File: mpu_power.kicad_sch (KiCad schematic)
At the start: 50 parts, among them U501 STM32MP135FAE7

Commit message: Rework text boxes
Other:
- note added: "Decoupling"
- note added: "Notes"
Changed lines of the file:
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@@
 		(rev "v1.0.0")
+	)
+	(rectangle
+		(start 12.7 251.46)
+		(end 298.45 284.48)
+		(stroke
+			(width 0)
+			(type default)
+		)
+		(fill
+			(type none)
+		)
+	)
+	(rectangle
+		(start 12.7 50.8)
+		(end 406.4 251.46)
+		(stroke
+			(width 0)
+			(type default)
+		)
+		(fill
+			(type none)
+		)
 	)
 	(text "1 µF x VDD"
@@
 		)
 	)
+	(text "Notes"
+		(exclude_from_sim no)
+		(at 13.97 254 0)
+		(effects
+			(font
+				(size 5.08 5.08)
+				(thickness 1.016)
+				(bold yes)
+			)
+			(justify left top)
+		)
+	)
 	(text "1 µF x VDD_PLL + 1 µF x VDD_SD2 + 1 µF x VBAT + 1 µF x VDD_ANA"
 		(exclude_from_sim no)
@@
 			)
 			(justify left bottom)
+		)
+	)
+	(text "Decoupling"
+		(exclude_from_sim no)
+		(at 13.97 53.34 0)
+		(effects
+			(font
+				(size 5.08 5.08)
+				(thickness 1.016)
+				(bold yes)
+			)
+			(justify left top)
 		)
 	)
@@
 		)
 	)
-	(text_box "Notes"
-		(exclude_from_sim no)
-		(at 12.7 251.46 0)
-		(size 285.75 33.02)
-		(margins 0.9525 2 0.9525 0.9525)
-		(stroke
-			(width 0)
-			(type solid)
-		)
-		(fill
-			(type none)
-		)
-		(effects
-			(font
-				(size 5.08 5.08)
-				(thickness 1.016)
-				(bold yes)
-			)
-			(justify top)
-		)
-	)
-	(text_box ""
-		(exclude_from_sim no)
-		(at 12.7 50.8 0)
-		(size 393.7 200.66)
-		(margins 0.9525 2 0.9525 0.9525)
-		(stroke
-			(width 0)
-			(type solid)
-		)
-		(fill
-			(type none)
-		)
-		(effects
-			(font
-				(size 5.08 5.08)
-				(thickness 1.016)
-				(bold yes)
-			)
-			(justify top)
-		)
-	)

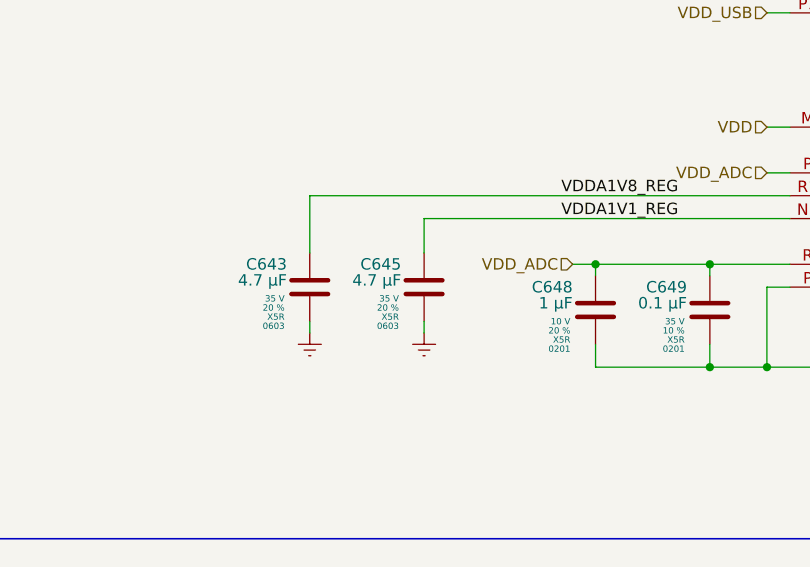
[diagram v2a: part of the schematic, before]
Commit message: Fix power connections
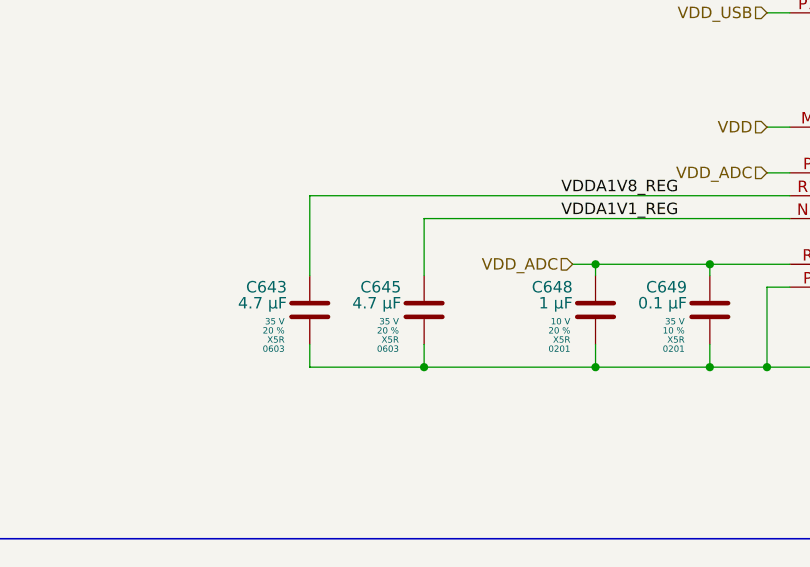
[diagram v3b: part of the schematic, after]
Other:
- moved on the sheet: C643, C645
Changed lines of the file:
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@@
 	)
 	(junction
+		(at 196.85 232.41)
+		(diameter 0)
+		(color 0 0 0 0)
+	)
+	(junction
 		(at 260.35 88.9)
 		(diameter 0)
@@
 	)
 	(junction
+		(at 177.8 232.41)
+		(diameter 0)
+		(color 0 0 0 0)
+	)
+	(junction
 		(at 53.34 177.8)
 		(diameter 0)
@@
 	(wire
 		(pts
-			(xy 177.8 215.9) (xy 177.8 219.71)
+			(xy 177.8 215.9) (xy 177.8 222.25)
 		)
 		(stroke
@@
 	(wire
 		(pts
+			(xy 165.1 232.41) (xy 177.8 232.41)
+		)
+		(stroke
+			(width 0)
+			(type default)
+		)
+	)
+	(wire
+		(pts
 			(xy 40.64 180.34) (xy 40.64 177.8)
 		)
@@
 	(wire
 		(pts
+			(xy 177.8 232.41) (xy 196.85 232.41)
+		)
+		(stroke
+			(width 0)
+			(type default)
+		)
+	)
+	(wire
+		(pts
 			(xy 78.74 165.1) (xy 91.44 165.1)
 		)
@@
 	(wire
 		(pts
+			(xy 165.1 229.87) (xy 165.1 232.41)
+		)
+		(stroke
+			(width 0)
+			(type default)
+		)
+	)
+	(wire
+		(pts
 			(xy 66.04 190.5) (xy 78.74 190.5)
 		)
@@
 	(wire
 		(pts
-			(xy 177.8 227.33) (xy 177.8 228.6)
+			(xy 177.8 229.87) (xy 177.8 232.41)
 		)
 		(stroke
@@
 	(wire
 		(pts
-			(xy 165.1 213.36) (xy 165.1 219.71)
+			(xy 165.1 213.36) (xy 165.1 222.25)
 		)
 		(stroke
@@
 	(wire
 		(pts
-			(xy 165.1 227.33) (xy 165.1 228.6)
-		)
-		(stroke
-			(width 0)
-			(type default)
-		)
-	)
-	(wire
-		(pts
 			(xy 209.55 229.87) (xy 209.55 232.41)
 		)
@@
 		(dnp no)
 		(fields_autoplaced yes)
-		(property "Reference" "#PWR0611"
+		(property "Reference" "#PWR0609"
 			(at 260.35 240.03 0)
 			(effects
@@
 			(project "linux-sbc"
 				(path "/fa11a02f-8043-4153-ab69-88d766503017/2d01087b-54dc-4f43-9cc7-a0ba17201776/38fb80ce-3aa2-4a17-bb8b-7759011755a2"
-					(reference "#PWR0611")
+					(reference "#PWR0609")
 					(unit 1)
 				)
@@
 	(symbol
 		(lib_id "Device:C")
-		(at 177.8 223.52 0)
+		(at 177.8 226.06 0)
 		(mirror y)
 		(unit 1)
@@
 		(dnp no)
 		(property "Reference" "C645"
-			(at 175.26 220.98 0)
+			(at 175.26 223.52 0)
 			(effects
 				(font
@@
 		)
 		(property "Value" "4.7 µF"
-			(at 175.26 222.758 0)
+			(at 175.26 225.298 0)
 			(effects
 				(font
@@
 		)
 		(property "Footprint" "Capacitor_SMD:C_0603_1608Metric"
-			(at 176.8348 227.33 0)
+			(at 176.8348 229.87 0)
 			(effects
 				(font
@@
 		)
 		(property "Datasheet" "https://search.murata.co.jp/Ceramy/image/img/A01X/G101/ENG/GRM188R6YA475KE15-01.pdf"
-			(at 177.8 223.52 0)
+			(at 177.8 226.06 0)
 			(effects
 				(font
@@
 		)
 		(property "Description" "4.7 µF ±10% 35V Ceramic Capacitor X5R 0603 (1608 Metric)"
-			(at 177.8 223.52 0)
+			(at 177.8 226.06 0)
 			(effects
 				(font
@@
 		)
 		(property "MPN" "GRM188R6YA475KE15D"
-			(at 177.8 223.52 0)
+			(at 177.8 226.06 0)
 			(effects
 				(font
@@
 		)
 		(property "Manufacturer" "Murata Electronics"
-			(at 177.8 223.52 0)
+			(at 177.8 226.06 0)
 			(effects
 				(font
@@
 		)
 		(property "Voltage rating" "35 V"
-			(at 175.006 224.79 0)
+			(at 175.006 227.33 0)
 			(effects
 				(font
@@
 		)
 		(property "Tolerance" "20 %"
-			(at 175.006 225.806 0)
+			(at 175.006 228.346 0)
 			(effects
 				(font
@@
 		)
 		(property "Temperature coefficient" "X5R"
-			(at 175.006 226.822 0)
+			(at 175.006 229.362 0)
 			(effects
 				(font
@@
 		)
 		(property "Size" "0603"
-			(at 175.006 227.838 0)
+			(at 175.006 230.378 0)
 			(effects
 				(font
@@
 		)
 		(property "Digi-Key Part Number" "490-7205-1-ND"
-			(at 177.8 223.52 0)
+			(at 177.8 226.06 0)
 			(effects
 				(font
@@
 	(symbol
 		(lib_id "Device:C")
-		(at 165.1 223.52 0)
+		(at 165.1 226.06 0)
 		(mirror y)
 		(unit 1)
@@
 		(dnp no)
 		(property "Reference" "C643"
-			(at 162.56 220.98 0)
+			(at 162.56 223.52 0)
 			(effects
 				(font
@@
 		)
 		(property "Value" "4.7 µF"
-			(at 162.56 222.758 0)
+			(at 162.56 225.298 0)
 			(effects
 				(font
@@
 		)
 		(property "Footprint" "Capacitor_SMD:C_0603_1608Metric"
-			(at 164.1348 227.33 0)
+			(at 164.1348 229.87 0)
 			(effects
 				(font
@@
 		)
 		(property "Datasheet" "https://search.murata.co.jp/Ceramy/image/img/A01X/G101/ENG/GRM188R6YA475KE15-01.pdf"
-			(at 165.1 223.52 0)
+			(at 165.1 226.06 0)
 			(effects
 				(font
@@
 		)
 		(property "Description" "4.7 µF ±10% 35V Ceramic Capacitor X5R 0603 (1608 Metric)"
-			(at 165.1 223.52 0)
+			(at 165.1 226.06 0)
 			(effects
 				(font
@@
 		)
 		(property "MPN" "GRM188R6YA475KE15D"
-			(at 165.1 223.52 0)
+			(at 165.1 226.06 0)
 			(effects
 				(font
@@
 		)
 		(property "Manufacturer" "Murata Electronics"
-			(at 165.1 223.52 0)
+			(at 165.1 226.06 0)
 			(effects
 				(font
@@
 		)
 		(property "Voltage rating" "35 V"
-			(at 162.306 224.79 0)
+			(at 162.306 227.33 0)
 			(effects
 				(font
@@
 		)
 		(property "Tolerance" "20 %"
-			(at 162.306 225.806 0)
+			(at 162.306 228.346 0)
 			(effects
 				(font
@@
 		)
 		(property "Temperature coefficient" "X5R"
-			(at 162.306 226.822 0)
+			(at 162.306 229.362 0)
 			(effects
 				(font
@@
 		)
 		(property "Size" "0603"
-			(at 162.306 227.838 0)
+			(at 162.306 230.378 0)
 			(effects
 				(font
@@
 		)
 		(property "Digi-Key Part Number" "490-7205-1-ND"
-			(at 165.1 223.52 0)
+			(at 165.1 226.06 0)
 			(effects
 				(font
@@
 	)
 	(symbol
-		(lib_id "power:Earth")
-		(at 177.8 228.6 0)
-		(unit 1)
-		(exclude_from_sim no)
-		(in_bom yes)
-		(on_board yes)
-		(dnp no)
-		(fields_autoplaced yes)
-		(property "Reference" "#PWR0609"
-			(at 177.8 234.95 0)
-			(effects
-				(font
-					(size 1.27 1.27)
-				)
-				(hide yes)
-			)
-		)
-		(property "Value" "GND"
-			(at 177.8 233.68 0)
-			(effects
-				(font
-					(size 1.27 1.27)
-				)
-				(hide yes)
-			)
-		)
-		(property "Footprint" ""
-			(at 177.8 228.6 0)
-			(effects
-				(font
-					(size 1.27 1.27)
-				)
-				(hide yes)
-			)
-		)
-		(property "Datasheet" "~"
-			(at 177.8 228.6 0)
-			(effects
-				(font
-					(size 1.27 1.27)
-				)
-				(hide yes)
-			)
-		)
-		(property "Description" "Power symbol creates a global label with name \"Earth\""
-			(at 177.8 228.6 0)
-			(effects
-				(font
-					(size 1.27 1.27)
-				)
-				(hide yes)
-			)
-		)
-		(pin "1"
-		)
-		(instances
-			(project "linux-sbc"
-				(path "/fa11a02f-8043-4153-ab69-88d766503017/2d01087b-54dc-4f43-9cc7-a0ba17201776/38fb80ce-3aa2-4a17-bb8b-7759011755a2"
-					(reference "#PWR0609")
-					(unit 1)
-				)
-			)
-		)
-	)
-	(symbol
 		(lib_id "STMicroelectronics:STM32MP135FAE7")
 		(at 238.76 214.63 0)
@@
 	)
 	(symbol
-		(lib_id "power:Earth")
-		(at 165.1 228.6 0)
-		(unit 1)
-		(exclude_from_sim no)
-		(in_bom yes)
-		(on_board yes)
-		(dnp no)
-		(fields_autoplaced yes)
-		(property "Reference" "#PWR0608"
-			(at 165.1 234.95 0)
-			(effects
-				(font
-					(size 1.27 1.27)
-				)
-				(hide yes)
-			)
-		)
-		(property "Value" "GND"
-			(at 165.1 233.68 0)
-			(effects
-				(font
-					(size 1.27 1.27)
-				)
-				(hide yes)
-			)
-		)
-		(property "Footprint" ""
-			(at 165.1 228.6 0)
-			(effects
-				(font
-					(size 1.27 1.27)
-				)
-				(hide yes)
-			)
-		)
-		(property "Datasheet" "~"
-			(at 165.1 228.6 0)
-			(effects
-				(font
-					(size 1.27 1.27)
-				)
-				(hide yes)
-			)
-		)
-		(property "Description" "Power symbol creates a global label with name \"Earth\""
-			(at 165.1 228.6 0)
-			(effects
-				(font
-					(size 1.27 1.27)
-				)
-				(hide yes)
-			)
-		)
-		(pin "1"
-		)
-		(instances
-			(project "linux-sbc"
-				(path "/fa11a02f-8043-4153-ab69-88d766503017/2d01087b-54dc-4f43-9cc7-a0ba17201776/38fb80ce-3aa2-4a17-bb8b-7759011755a2"
-					(reference "#PWR0608")
-					(unit 1)
-				)
-			)
-		)
-	)
-	(symbol
 		(lib_id "Device:C")
 		(at 66.04 158.75 0)
@@
 		(dnp no)
 		(fields_autoplaced yes)
-		(property "Reference" "#PWR0610"
+		(property "Reference" "#PWR0608"
 			(at 196.85 130.81 0)
 			(effects
@@
 			(project "linux-sbc"
 				(path "/fa11a02f-8043-4153-ab69-88d766503017/2d01087b-54dc-4f43-9cc7-a0ba17201776/38fb80ce-3aa2-4a17-bb8b-7759011755a2"
-					(reference "#PWR0610")
+					(reference "#PWR0608")
 					(unit 1)
 				)

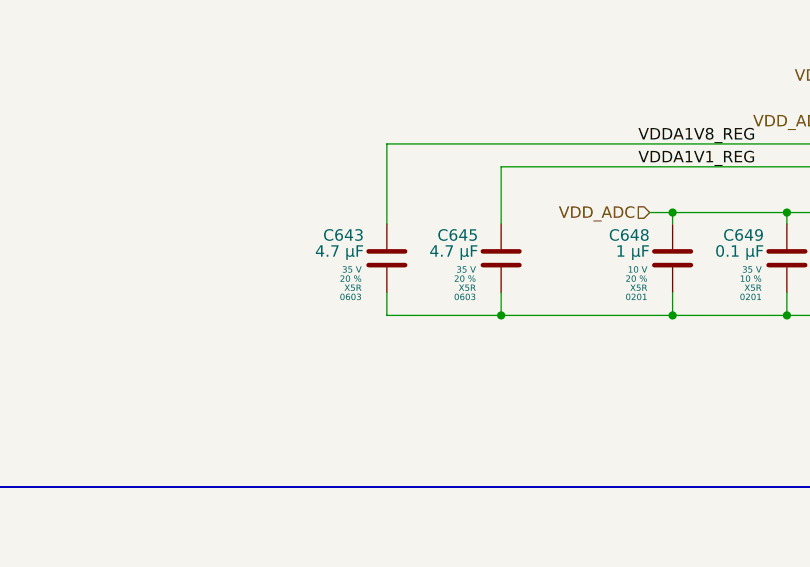
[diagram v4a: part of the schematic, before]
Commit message: Place MPU decoupling
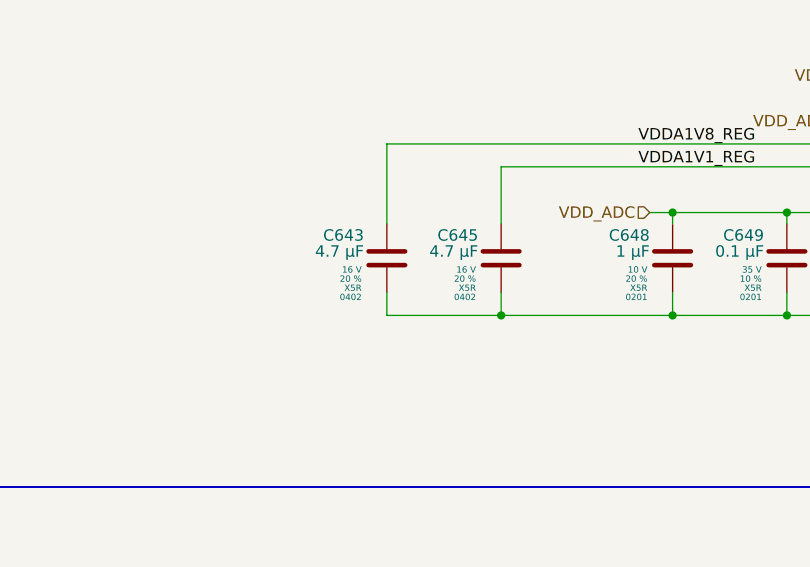
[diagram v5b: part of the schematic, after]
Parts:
- C643, C645: footprint Capacitor_SMD:C_0603_1608Metric -> perfect_footprints:C_0402_1005Metric; Digi-Key Part Number 490-7205-1-ND -> 1276-6836-1-ND; MPN GRM188R6YA475KE15D -> CL05A475MO5NUNC; Manufacturer Murata Electronics -> Samsung Electro-Mechanics; Size 0603 -> 0402; Voltage rating 35 V -> 16 V

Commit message: Update 0402 footprints
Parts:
- C643, C645: footprint perfect_footprints:C_0402_1005Metric -> perfect_footprints:C_0402_1005Metric_HDI
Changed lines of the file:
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@@
 			)
 		)
-		(property "Footprint" "perfect_footprints:C_0402_1005Metric"
+		(property "Footprint" "perfect_footprints:C_0402_1005Metric_HDI"
 			(at 164.1348 229.87 0)
 			(effects
@@
 			)
 		)
-		(property "Footprint" "perfect_footprints:C_0402_1005Metric"
+		(property "Footprint" "perfect_footprints:C_0402_1005Metric_HDI"
 			(at 176.8348 229.87 0)
 			(effects
